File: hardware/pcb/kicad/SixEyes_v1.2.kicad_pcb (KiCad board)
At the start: 4 copper layers, 44.8 x 58.4 mm, 49 parts, among them M1 NEMA17 40mm, U1 AS5600 Module

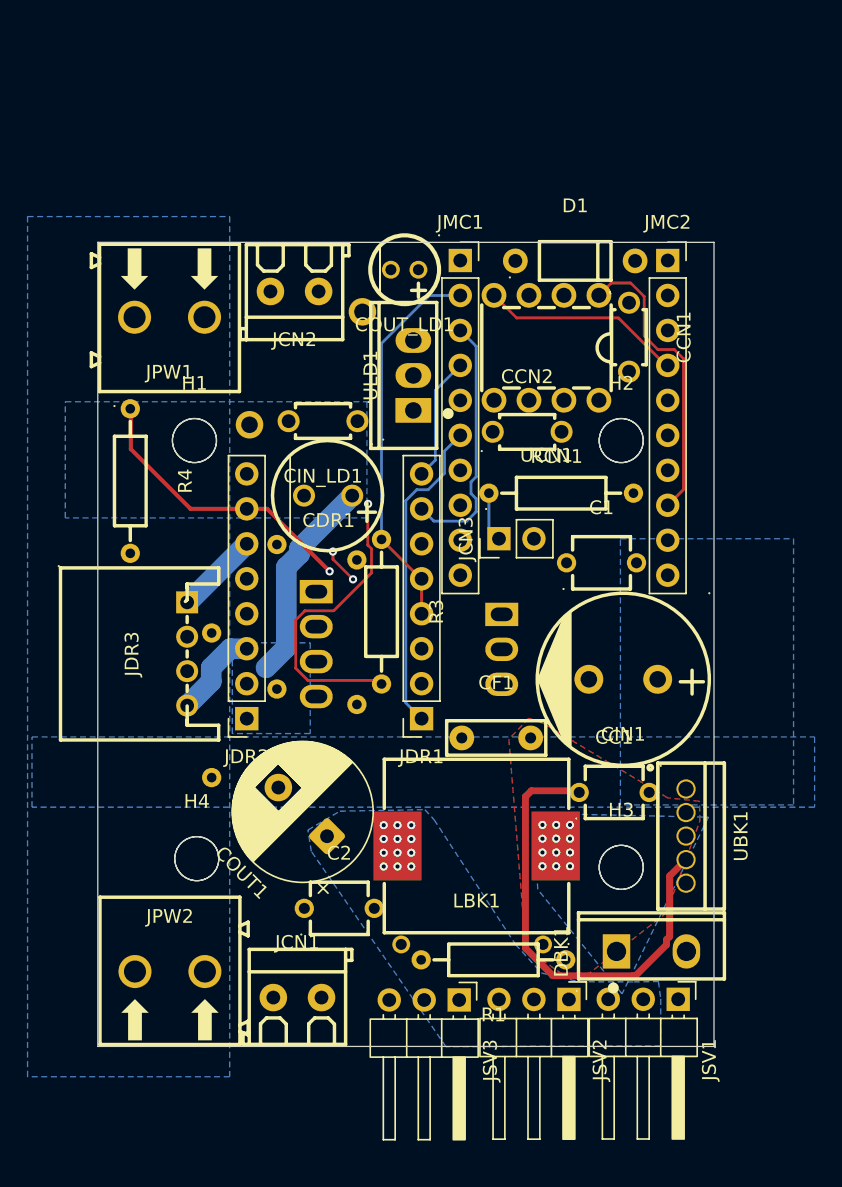
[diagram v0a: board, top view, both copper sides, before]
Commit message: Update the joint board for UART mode and the new pin map
MS1 and MS2 move to GPIO15 and GPIO16, UART TX to GPIO5, and the module's VREF
pad is read on GPIO2 through a new 10k resistor (R5). Adds the JDR4 socket for
the module's VREF and DIAG pads, VM and EN markers, a corrected regulator label,
JLCPCB 4-layer stackup and limits, net classes, and custom design rules for
power track widths, via sizes and the CAN pair. BOM gains the second 10k
resistor and JDR4.
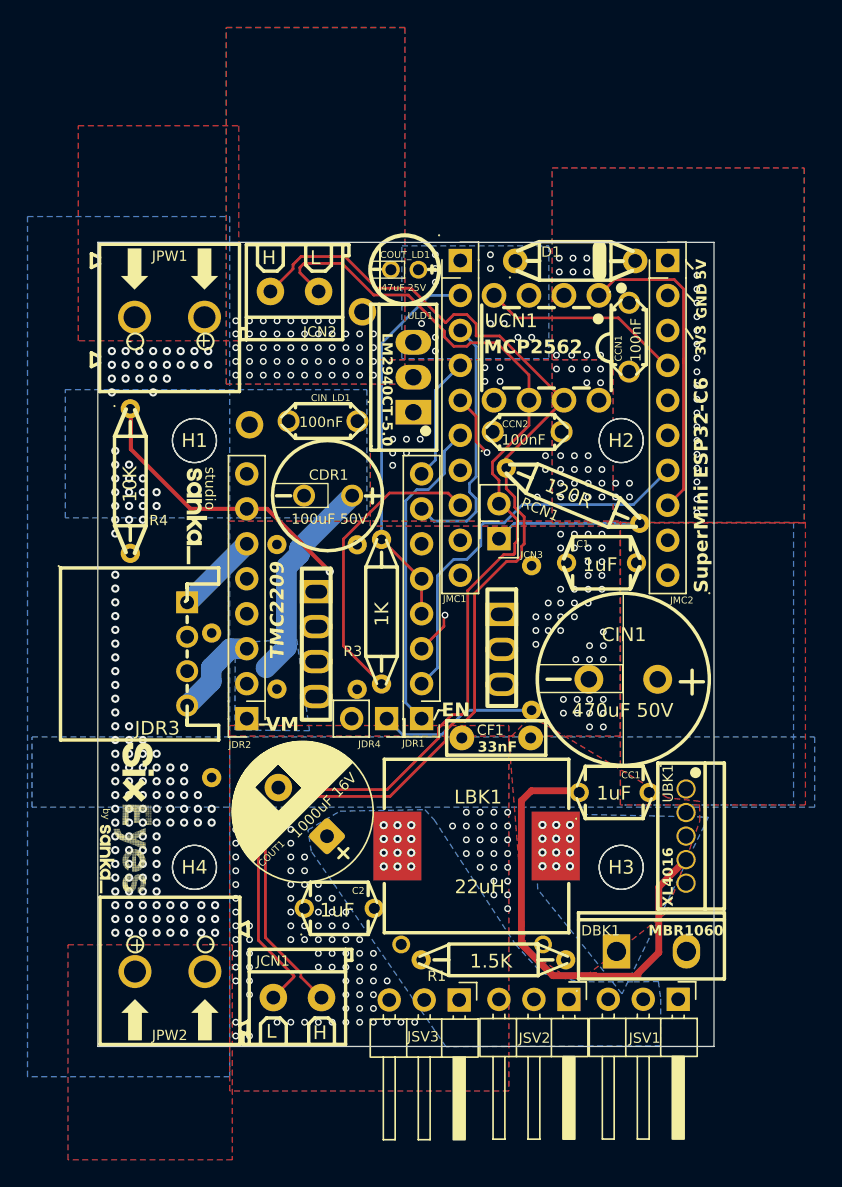
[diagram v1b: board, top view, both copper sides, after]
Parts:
- added G***: LOGO, LOGO, F.Cu at (128.1, 144.9)
- added G***: LOGO, LOGO, F.Cu at (130.1, 141.9)
- added G***: LOGO, LOGO, F.Cu at (134.6, 120.0)
- added G***: LOGO, LOGO, B.Cu at (160.1, 106.4)
- added JDR4: Conn_01x02, Connector_PinSocket_2.54mm:PinSocket_1x02_P2.54mm_Vertical, F.Cu at (148.5, 134.7)
- added R5: MF1/4W-10KΩ±1% T52, SixEyes_v1.2:RES-TH_BD2.3-L6.5-P10.50-D0.5, B.Cu at (159.0, 128.8)
- moved RSV1 1.10 mm to (146.3, 127.3)
- moved RCN1 0.88 mm to (162.0, 118.5), turned to 157.5 degrees
- moved H4 0.65 mm to (134.5, 145.5)
- moved SO4 0.65 mm to (134.5, 145.5)
- moved ULD1 0.13 mm to (150.4, 109.9)
- turned JCN3 to 180 degrees
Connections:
- net Net-(D1-K) renamed /5V_PAD
- JCN1 pad 1: /CANH -> /CAN-
- JCN1 pad 2: /CANL -> /CAN+
- JCN2 pad 1: /CANH -> /CAN-
- JCN2 pad 2: /CANL -> /CAN+
- JCN3 pad 2: /CANL- -> /CAN-
- JDR1 pad 2: GND -> /MS1
- JDR1 pad 3: GND -> /MS2
- JMC1 pad 1: unconnected-(JMC1-Pin_1-Pad1) -> /MS2
- JMC1 pad 5: /UART_TX -> /VREF_ADC
- JMC1 pad 8: unconnected-(JMC1-Pin_8-Pad8) -> /UART_TX
- JMC2 pad 7: unconnected-(JMC2-Pin_7-Pad7) -> /MS1
- RCN1 pad 2: /CANH+ -> /CAN+
- UCN1 pad 6: /CANL- -> /CAN-
- UCN1 pad 7: /CANH+ -> /CAN+
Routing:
- net /CAN+: track 0.00 -> 87.4 mm
- net /CAN-: track 0.00 -> 83.9 mm
- net /MS2: track 0.00 -> 31.3 mm, vias 0 -> 1
- net /MS1: track 0.00 -> 29.1 mm
- net /VREF_ADC: track 0.00 -> 14.2 mm, vias 0 -> 1
- net /UART_TX: track 35.6 -> 21.9 mm, vias 1 -> 0
- net /VREF_DR: track 0.00 -> 11.7 mm
- net Net-(JCN3-Pin_1): track 3.61 -> 11.7 mm
- net /SCL: track 40.0 -> 43.1 mm
- net /PWM3: track 23.6 -> 26.5 mm
- net /SDA: track 41.3 -> 43.4 mm
- net /CAN_TX	: track 21.6 -> 23.4 mm
- net +3V3: track 69.2 -> 70.7 mm
- net Net-(JSV1-Pin_1): track 40.4 -> 41.6 mm
- net /PWM2: track 15.7 -> 15.4 mm, vias 2 -> 0
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- added copper zone on B.Cu, net +5V
- added copper zone on B.Cu, net GND
- added copper zone on F.Cu, net GND
- added copper zone on In2.Cu, net GND
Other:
- board text added: "+"
- board text added: "-"
- board text added: "1.5K"
- board text added: "1000uF 16V"
- board text added: "100nF"
- board text added: "100uF 50V"
- board text added: "10K"
- board text added: "120R"
- board text added: "1K"
- board text added: "1uF"
- board text added: "22uH"
- board text added: "33nF"
- board text added: "3V3"
- board text added: "470uF 50V"
- board text added: "47uF 25V"
- board text added: "5V"
- board text added: "6.2K"
- board text added: "EN"
- board text added: "GND"
- board text added: "H"
- board text added: "L"
- board text added: "LM2940CT-5.0"
- board text added: "MBR1060"
- board text added: "MCP2562"
- board text added: "P6KE30A"
- board text added: "SuperMini ESP32-C6"
- board text added: "TMC2209"
- board text added: "VM"
- board text added: "XL4016"
- board text added: "by"
- board text added: "studio"

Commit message: Release PCB v1.2: Studio Sanka title block, signed drawings, fabrication files
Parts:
- removed H1, H2, H3, H4: MountingHole, MountingHole:MountingHole_3.2mm_M3
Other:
- board text added: "(c) 2026 Studio Sanka"
- board text added: "CERN-OHL-S-2.0"
- board text added: "SXE-PCB v1.2"
- board text added: "github.com/studiosanka/sixeyes"

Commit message: Update fabrication files and drawings for the terminal pinout silkscreen; add board renders to the docs
Regenerated Gerber zip (new checksum), re-signed layout PDF, bare-board and assembly renders in the guides and READMEs, budget scope now excludes shipping, PCB quote added.
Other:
- board text added: "+24V"
- board text added: "6.5V"
- board text added: "CANH"
- board text added: "CANL"
- board text added: "PWM"
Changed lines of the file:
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@@
 		(pcbplotparams
 			(layerselection 0x00000000_00000000_55555555_575555ff)
-			(plot_on_all_layers_selection 0x00000000_00000000_00000000_00000000)
+			(plot_on_all_layers_selection 0x00000000_00000000_00000000_02000000)
 			(disableapertmacros no)
 			(usegerberextensions no)
@@
 			(dashed_line_gap_ratio 3)
 			(svgprecision 4)
-			(plotframeref no)
+			(plotframeref yes)
 			(mode 1)
 			(useauxorigin no)
@@
 			(pdf_back_fp_property_popups yes)
 			(pdf_metadata yes)
-			(pdf_single_document no)
+			(pdf_single_document yes)
 			(dxfpolygonmode yes)
 			(dxfimperialunits yes)
@@
 			(psnegative no)
 			(psa4output no)
-			(plot_black_and_white yes)
+			(plot_black_and_white no)
 			(sketchpadsonfab no)
 			(plotpadnumbers no)
@@
 			(crossoutdnponfab yes)
 			(subtractmaskfromsilk yes)
-			(outputformat 1)
+			(outputformat 4)
 			(mirror no)
-			(drillshape 0)
+			(drillshape 2)
 			(scaleselection 1)
 			(outputdirectory "../gerbers/")
@@
 		)
 	)
+	(gr_text "GND\n"
+		(locked yes)
+		(at 148.21 158.57 270)
+		(layer "B.SilkS")
+		(effects
+			(font
+				(size 0.75 0.75)
+				(thickness 0.1875)
+				(bold yes)
+			)
+			(justify left bottom mirror)
+		)
+	)
+	(gr_text "6.5V"
+		(locked yes)
+		(at 150.62 158.58 270)
+		(layer "B.SilkS")
+		(effects
+			(font
+				(size 0.75 0.75)
+				(thickness 0.1875)
+				(bold yes)
+			)
+			(justify left bottom mirror)
+		)
+	)
+	(gr_text "PWM\n"
+		(locked yes)
+		(at 153.22 158.58 270)
+		(layer "B.SilkS")
+		(effects
+			(font
+				(size 0.75 0.75)
+				(thickness 0.1875)
+				(bold yes)
+			)
+			(justify left bottom mirror)
+		)
+	)
+	(gr_text "GND\n"
+		(locked yes)
+		(at 156.13 158.57 270)
+		(layer "B.SilkS")
+		(effects
+			(font
+				(size 0.75 0.75)
+				(thickness 0.1875)
+				(bold yes)
+			)
+			(justify left bottom mirror)
+		)
+	)
+	(gr_text "6.5V"
+		(locked yes)
+		(at 158.64 158.59 270)
+		(layer "B.SilkS")
+		(effects
+			(font
+				(size 0.75 0.75)
+				(thickness 0.1875)
+				(bold yes)
+			)
+			(justify left bottom mirror)
+		)
+	)
+	(gr_text "PWM\n"
+		(locked yes)
+		(at 161.24 158.59 270)
+		(layer "B.SilkS")
+		(effects
+			(font
+				(size 0.75 0.75)
+				(thickness 0.1875)
+				(bold yes)
+			)
+			(justify left bottom mirror)
+		)
+	)
+	(gr_text "GND\n"
+		(locked yes)
+		(at 164.14 158.56 270)
+		(layer "B.SilkS")
+		(effects
+			(font
+				(size 0.75 0.75)
+				(thickness 0.1875)
+				(bold yes)
+			)
+			(justify left bottom mirror)
+		)
+	)
+	(gr_text "6.5V"
+		(locked yes)
+		(at 166.55 158.57 270)
+		(layer "B.SilkS")
+		(effects
+			(font
+				(size 0.75 0.75)
+				(thickness 0.1875)
+				(bold yes)
+			)
+			(justify left bottom mirror)
+		)
+	)
+	(gr_text "PWM\n"
+		(locked yes)
+		(at 169.17 158.41 270)
+		(layer "B.SilkS")
+		(effects
+			(font
+				(size 0.75 0.75)
+				(thickness 0.1875)
+				(bold yes)
+			)
+			(justify left bottom mirror)
+		)
+	)
 	(gr_text "CERN-OHL-S-2.0 \n\n"
 		(locked yes)
-		(at 141.43 159.65 0)
+		(at 152.95 155.37 0)
 		(layer "B.SilkS")
 		(effects
@@
 	(gr_text "(c) 2026 Studio Sanka"
 		(locked yes)
-		(at 143.79 156.81 0)
+		(at 170.33 153.93 0)
 		(layer "B.SilkS")
 		(effects
@@
 		)
 	)
-	(gr_text "6.2K"
+	(gr_text "GND\n"
 		(locked yes)
-		(at 156.3 151.7 0)
+		(at 130.759999 100.249999 90)
 		(layer "B.SilkS")
 		(effects
 			(font
-				(size 1 1)
-				(thickness 0.15)
+				(size 0.85 0.85)
+				(thickness 0.2125)
+				(bold yes)
 			)
 			(justify left bottom mirror)
 		)
 	)
-	(gr_text "1K"
+	(gr_text "+24V"
 		(locked yes)
-		(at 136.3 132.6 90)
+		(at 135.72 100.41 90)
 		(layer "B.SilkS")
 		(effects
 			(font
-				(size 1 1)
-				(thickness 0.15)
+				(size 0.85 0.85)
+				(thickness 0.2125)
+				(bold yes)
 			)
 			(justify left bottom mirror)
 		)
 	)
-	(gr_text "1K"
+	(gr_text "CANH\n"
 		(locked yes)
-		(at 141 126.1 90)
+		(at 142.14 100.22 90)
 		(layer "B.SilkS")
 		(effects
 			(font
-				(size 1 1)
-				(thickness 0.15)
+				(size 0.85 0.85)
+				(thickness 0.2125)
+				(bold yes)
 			)
 			(justify left bottom mirror)
 		)
 	)
-	(gr_text "1K"
+	(gr_text "CANL"
 		(locked yes)
-		(at 146.9 127.3 90)
+		(at 145.560001 100.100002 90)
+		(layer "B.SilkS")
+		(effects
+			(font
+				(size 0.85 0.85)
+				(thickness 0.2125)
+				(bold yes)
+			)
+			(justify left bottom mirror)
+		)
+	)
+	(gr_text "+24V"
+		(locked yes)
+		(at 129.81 157.98 270)
+		(layer "B.SilkS")
+		(effects
+			(font
+				(size 0.85 0.85)
+				(thickness 0.2125)
+				(bold yes)
+			)
+			(justify left bottom mirror)
+		)
+	)
+	(gr_text "GND\n"
+		(locked yes)
+		(at 134.77 158.14 270)
+		(layer "B.SilkS")
+		(effects
+			(font
+				(size 0.85 0.85)
+				(thickness 0.2125)
+				(bold yes)
+			)
+			(justify left bottom mirror)
+		)
+	)
+	(gr_text "CANL"
+		(locked yes)
+		(at 138.28 158.46 270)
+		(layer "B.SilkS")
+		(effects
+			(font
+				(size 0.85 0.85)
+				(thickness 0.2125)
+				(bold yes)
+			)
+			(justify left bottom mirror)
+		)
+	)
+	(gr_text "CANH\n"
+		(locked yes)
+		(at 141.61 158.45 270)
+		(layer "B.SilkS")
+		(effects
+			(font
+				(size 0.85 0.85)
+				(thickness 0.2125)
+				(bold yes)
+			)
+			(justify left bottom mirror)
+		)
+	)
+	(gr_text "github.com/studiosanka/sixeyes"
+		(locked yes)
+		(at 161.82 138.53 0)
+		(layer "B.SilkS")
+		(effects
+			(font
+				(size 0.95 0.95)
+				(thickness 0.2375)
+				(bold yes)
+			)
+			(justify left bottom mirror)
+		)
+	)
+	(gr_text "6.2K"
+		(locked yes)
+		(at 156.3 151.7 0)
 		(layer "B.SilkS")
 		(effects
@@
 		)
 	)
-	(gr_text "10K\n"
+	(gr_text "1K"
 		(locked yes)
-		(at 160.1 127.6 90)
+		(at 136.3 132.6 90)
 		(layer "B.SilkS")
 		(effects
@@
 		)
 	)
-	(gr_text "CERN-OHL-S-2.0 \n\n"
+	(gr_text "1K"
 		(locked yes)
-		(at 156.61 142.11 0)
+		(at 141 126.1 90)
 		(layer "B.SilkS")
 		(effects
 			(font
 				(size 1 1)
-				(thickness 0.25)
-				(bold yes)
+				(thickness 0.15)
 			)
 			(justify left bottom mirror)
 		)
 	)
-	(gr_text "(c) 2026 Studio Sanka"
+	(gr_text "1K"
 		(locked yes)
-		(at 159.33 138.67 0)
+		(at 146.9 127.3 90)
 		(layer "B.SilkS")
 		(effects
 			(font
 				(size 1 1)
-				(thickness 0.25)
-				(bold yes)
+				(thickness 0.15)
 			)
 			(justify left bottom mirror)
 		)
 	)
-	(gr_text "github.com/studiosanka/sixeyes"
+	(gr_text "10K\n"
 		(locked yes)
-		(at 170.48 157.4 0)
+		(at 160.1 127.6 90)
 		(layer "B.SilkS")
 		(effects
 			(font
 				(size 1 1)
-				(thickness 0.25)
-				(bold yes)
+				(thickness 0.15)
 			)
 			(justify left bottom mirror)
@@
 	(gr_text "SXE-PCB v1.2"
 		(locked yes)
-		(at 142.45 102.87 0)
+		(at 140.83 108.55 0)
 		(layer "B.SilkS")
 		(effects
